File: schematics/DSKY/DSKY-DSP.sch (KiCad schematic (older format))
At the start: 0 parts

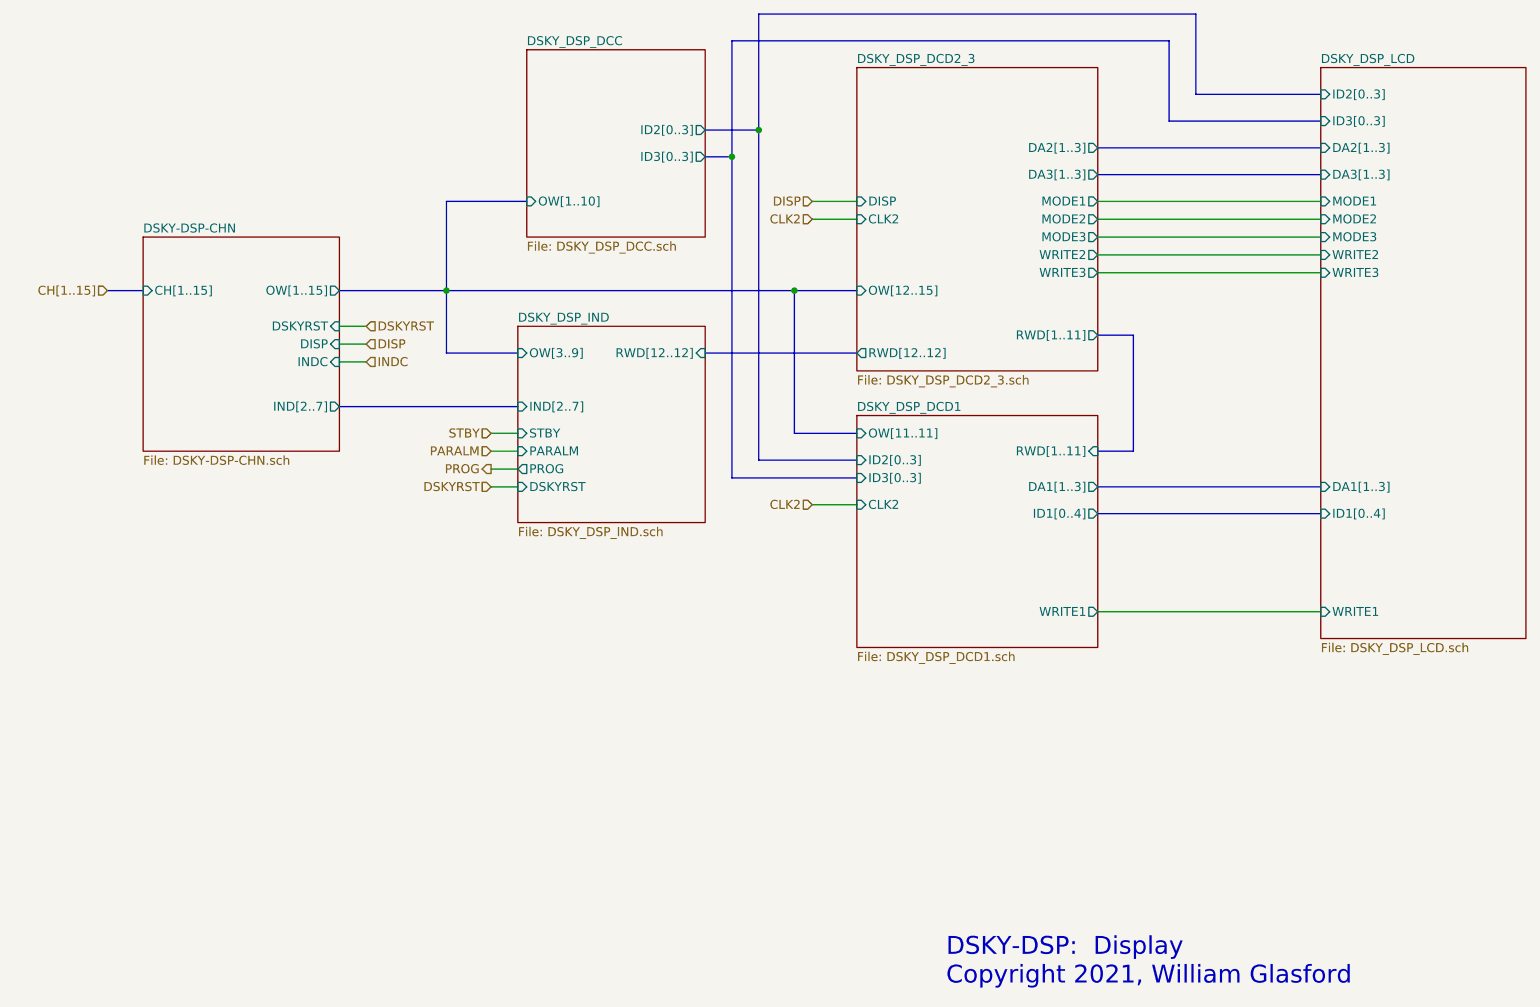
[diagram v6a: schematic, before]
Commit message: Sign processing overhauled.
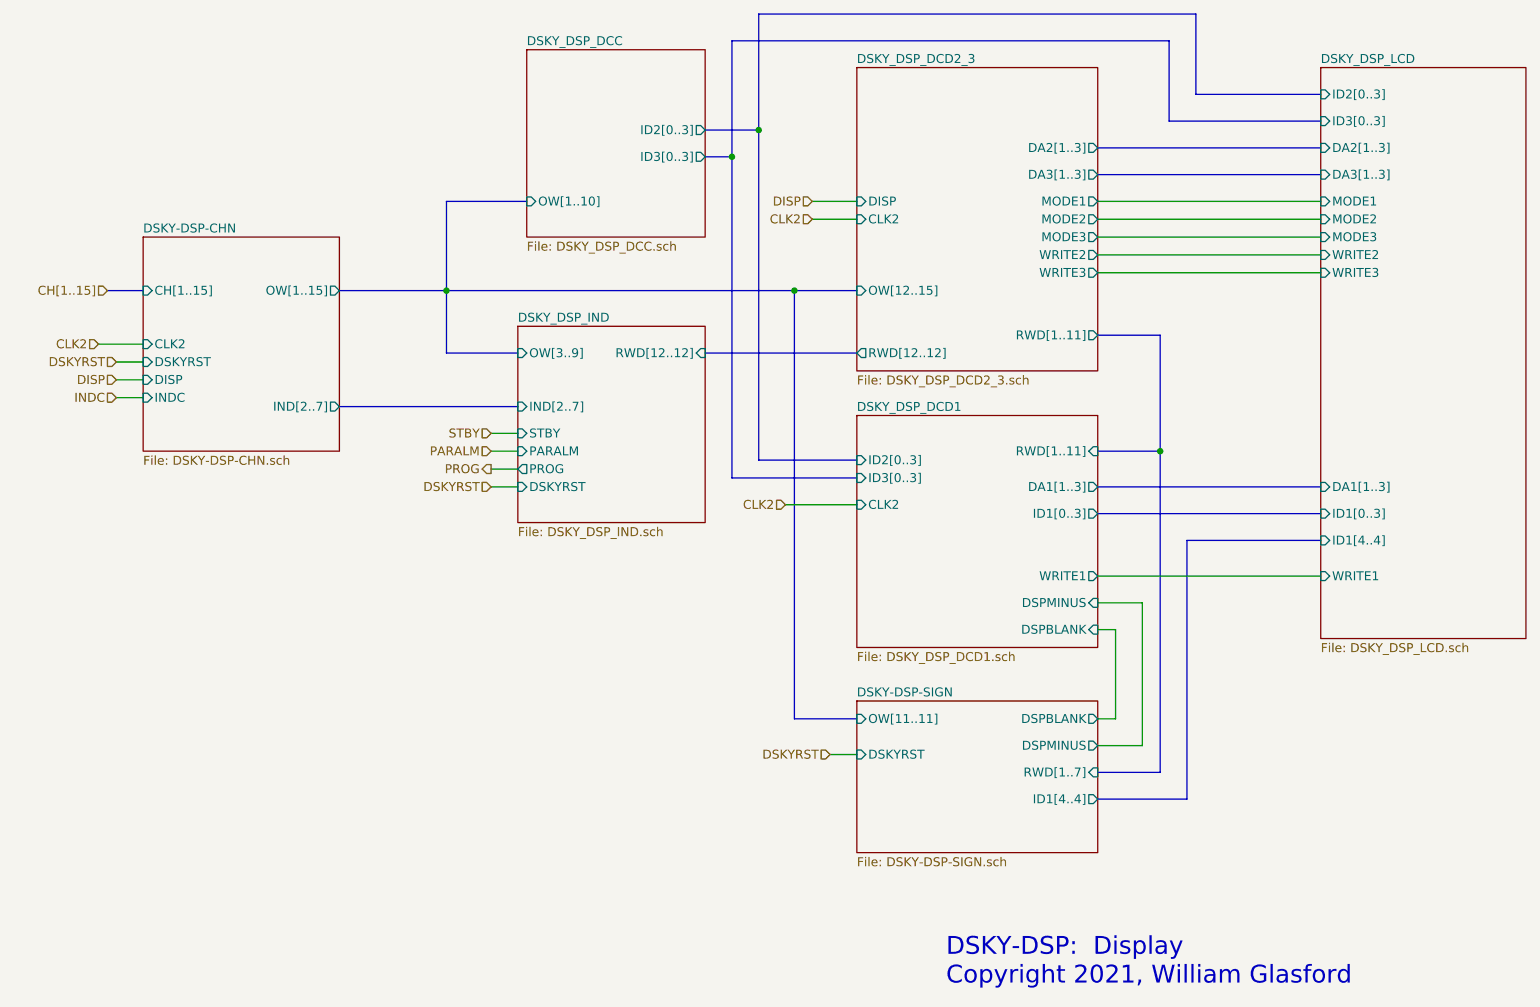
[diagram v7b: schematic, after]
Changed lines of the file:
@@
 $Descr A 11000 8500
 encoding utf-8
-Sheet 2 10
+Sheet 2 11
 Title ""
 Date ""
@@
 F3 "IND[2..7]" O R 2950 3900 50
 F4 "CH[1..15]" I L 1850 3250 50
-F5 "DSKYRST" I R 2950 3450 50
-F6 "DISP" I R 2950 3550 50
-F7 "INDC" I R 2950 3650 50
+F5 "DSKYRST" I L 1850 3650 50
+F6 "DISP" I L 1850 3750 50
+F7 "INDC" I L 1850 3850 50
+F8 "CLK2" I L 1850 3550 50
 $EndSheet
 Text HLabel 3800 4050 0    50   Input ~ 0
@@
 	2950 3250 3550 3250
 Wire Wire Line
-	3100 3550 2950 3550
-Text HLabel 3100 3450 2    50   Input ~ 0
+	1850 3750 1700 3750
+Text HLabel 1700 3650 0    50   Input ~ 0
 DSKYRST
 Wire Wire Line
-	2950 3450 3100 3450
-Wire Wire Line
-	3100 3650 2950 3650
-Text HLabel 3100 3550 2    50   Input ~ 0
+	1700 3650 1850 3650
+Wire Wire Line
+	1850 3850 1700 3850
+Text HLabel 1700 3750 0    50   Input ~ 0
 DISP
-Text HLabel 3100 3650 2    50   Input ~ 0
+Text HLabel 1700 3850 0    50   Input ~ 0
 INDC
 Wire Bus Line
@@
 	3550 3250 3550 3600
 Wire Wire Line
-	7200 5050 8450 5050
+	7200 4850 8450 4850
 Wire Bus Line
 	7200 2600 8450 2600
@@
 	7200 2450 8450 2450
 Wire Bus Line
-	7200 3500 7400 3500
-Wire Bus Line
-	7400 3500 7400 4150
-Wire Bus Line
-	7400 4150 7200 4150
+	7200 3500 7550 3500
+Wire Bus Line
+	7550 4150 7200 4150
 Wire Bus Line
 	5000 3600 5850 3600
 Wire Bus Line
 	2950 3900 3950 3900
-$Sheet
-S 5850 3950 1350 1300
-U 64844A8A
-F0 "DSKY_DSP_DCD1" 50
-F1 "DSKY_DSP_DCD1.sch" 50
-F2 "DA1[1..3]" O R 7200 4350 50
-F3 "ID1[0..4]" O R 7200 4500 50
-F4 "WRITE1" O R 7200 5050 50
-F5 "RWD[1..11]" I R 7200 4150 50
-F6 "ID3[0..3]" I L 5850 4300 50
-F7 "OW[11..11]" I L 5850 4050 50
-F8 "CLK2" I L 5850 4450 50
-F9 "ID2[0..3]" I L 5850 4200 50
-$EndSheet
 Wire Bus Line
 	5150 4300 5150 2500
@@
 	3550 3250 5500 3250
 Wire Bus Line
-	5500 3250 5500 4050
-Wire Bus Line
-	5500 4050 5850 4050
+	5500 3250 5500 5650
 Connection ~ 5500 3250
 Wire Bus Line
 	5500 3250 5850 3250
 Wire Wire Line
-	5850 4450 5600 4450
-Text HLabel 5600 4450 0    50   Input ~ 0
+	5850 4450 5450 4450
+Text HLabel 5450 4450 0    50   Input ~ 0
 CLK2
 Wire Bus Line
@@
 F2 "DA1[1..3]" I L 8450 4350 50
 F3 "ID2[0..3]" I L 8450 2150 50
-F4 "WRITE1" I L 8450 5050 50
+F4 "WRITE1" I L 8450 4850 50
 F5 "WRITE2" I L 8450 3050 50
 F6 "WRITE3" I L 8450 3150 50
-F7 "ID1[0..4]" I L 8450 4500 50
+F7 "ID1[0..3]" I L 8450 4500 50
 F8 "ID3[0..3]" I L 8450 2300 50
 F9 "DA2[1..3]" I L 8450 2450 50
@@
 F12 "MODE2" I L 8450 2850 50
 F13 "MODE3" I L 8450 2950 50
+F14 "ID1[4..4]" I L 8450 4650 50
 $EndSheet
 $Sheet
@@
 Wire Wire Line
 	3800 4350 3950 4350
+Wire Wire Line
+	1850 3550 1600 3550
+Text HLabel 1600 3550 0    50   Input ~ 0
+CLK2
+Wire Bus Line
+	5500 5650 5850 5650
+Wire Bus Line
+	8450 4650 7700 4650
+Wire Bus Line
+	7700 4650 7700 6100
+Text HLabel 5700 5850 0    50   Input ~ 0
+DSKYRST
+Wire Wire Line
+	5700 5850 5850 5850
+Wire Bus Line
+	7550 3500 7550 4150
+Connection ~ 7550 4150
+Wire Bus Line
+	7550 4150 7550 5950
+Wire Bus Line
+	7550 5950 7200 5950
+Wire Bus Line
+	7700 6100 7200 6100
+Wire Wire Line
+	7200 5150 7300 5150
+Wire Wire Line
+	7300 5150 7300 5650
+Wire Wire Line
+	7300 5650 7200 5650
+Wire Wire Line
+	7200 5800 7450 5800
+Wire Wire Line
+	7450 5800 7450 5000
+Wire Wire Line
+	7450 5000 7200 5000
+$Sheet
+S 5850 3950 1350 1300
+U 64844A8A
+F0 "DSKY_DSP_DCD1" 50
+F1 "DSKY_DSP_DCD1.sch" 50
+F2 "DA1[1..3]" O R 7200 4350 50
+F3 "ID1[0..3]" O R 7200 4500 50
+F4 "WRITE1" O R 7200 4850 50
+F5 "RWD[1..11]" I R 7200 4150 50
+F6 "ID3[0..3]" I L 5850 4300 50
+F7 "CLK2" I L 5850 4450 50
+F8 "ID2[0..3]" I L 5850 4200 50
+F9 "DSPMINUS" I R 7200 5000 50
+F10 "DSPBLANK" I R 7200 5150 50
+$EndSheet
+$Sheet
+S 5850 5550 1350 850
+U 61C9EF7C
+F0 "DSKY-DSP-SIGN" 50
+F1 "DSKY-DSP-SIGN.sch" 50
+F2 "OW[11..11]" I L 5850 5650 50
+F3 "ID1[4..4]" O R 7200 6100 50
+F4 "RWD[1..7]" I R 7200 5950 50
+F5 "DSKYRST" I L 5850 5850 50
+F6 "DSPBLANK" O R 7200 5650 50
+F7 "DSPMINUS" O R 7200 5800 50
+$EndSheet
 $EndSCHEMATC

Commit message: Overhauled the handling of the sign characters.
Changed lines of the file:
@@
 F6 "DSPBLANK" O R 7200 5650 50
 F7 "DSPMINUS" O R 7200 5800 50
+F8 "SGN_CLK2" I L 5850 5950 50
 $EndSheet
+Wire Wire Line
+	5850 5950 5700 5950
+Text HLabel 5700 5950 0    50   Input ~ 0
+SGN_CLK2
 $EndSCHEMATC
